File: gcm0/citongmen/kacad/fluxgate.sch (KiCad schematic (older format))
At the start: 81 parts, among them J1 +12, J11 SWD, J2 ji_li, Q1 BC547, Q10 KIA50N03, Q11 BC547, Q12 BC557, Q13 BC557, Q14 BC547, Q15 BC557, Q16 BC547, Q17 BC547, Q18 BC547, Q19 BC547, Q2 BC557, Q3 BC547, Q4 BC557, Q5 BC547, Q6 BC557, Q7 KIA50N03, Q8 KIA50N03, Q9 KIA50N03, U1 LM7809_TO220, U2 LM2596S-5, U3 LM7805_TO220, U5 STM32F030F4P6, U6 LM1117-3.3, U9 74HC595, Y1 8M

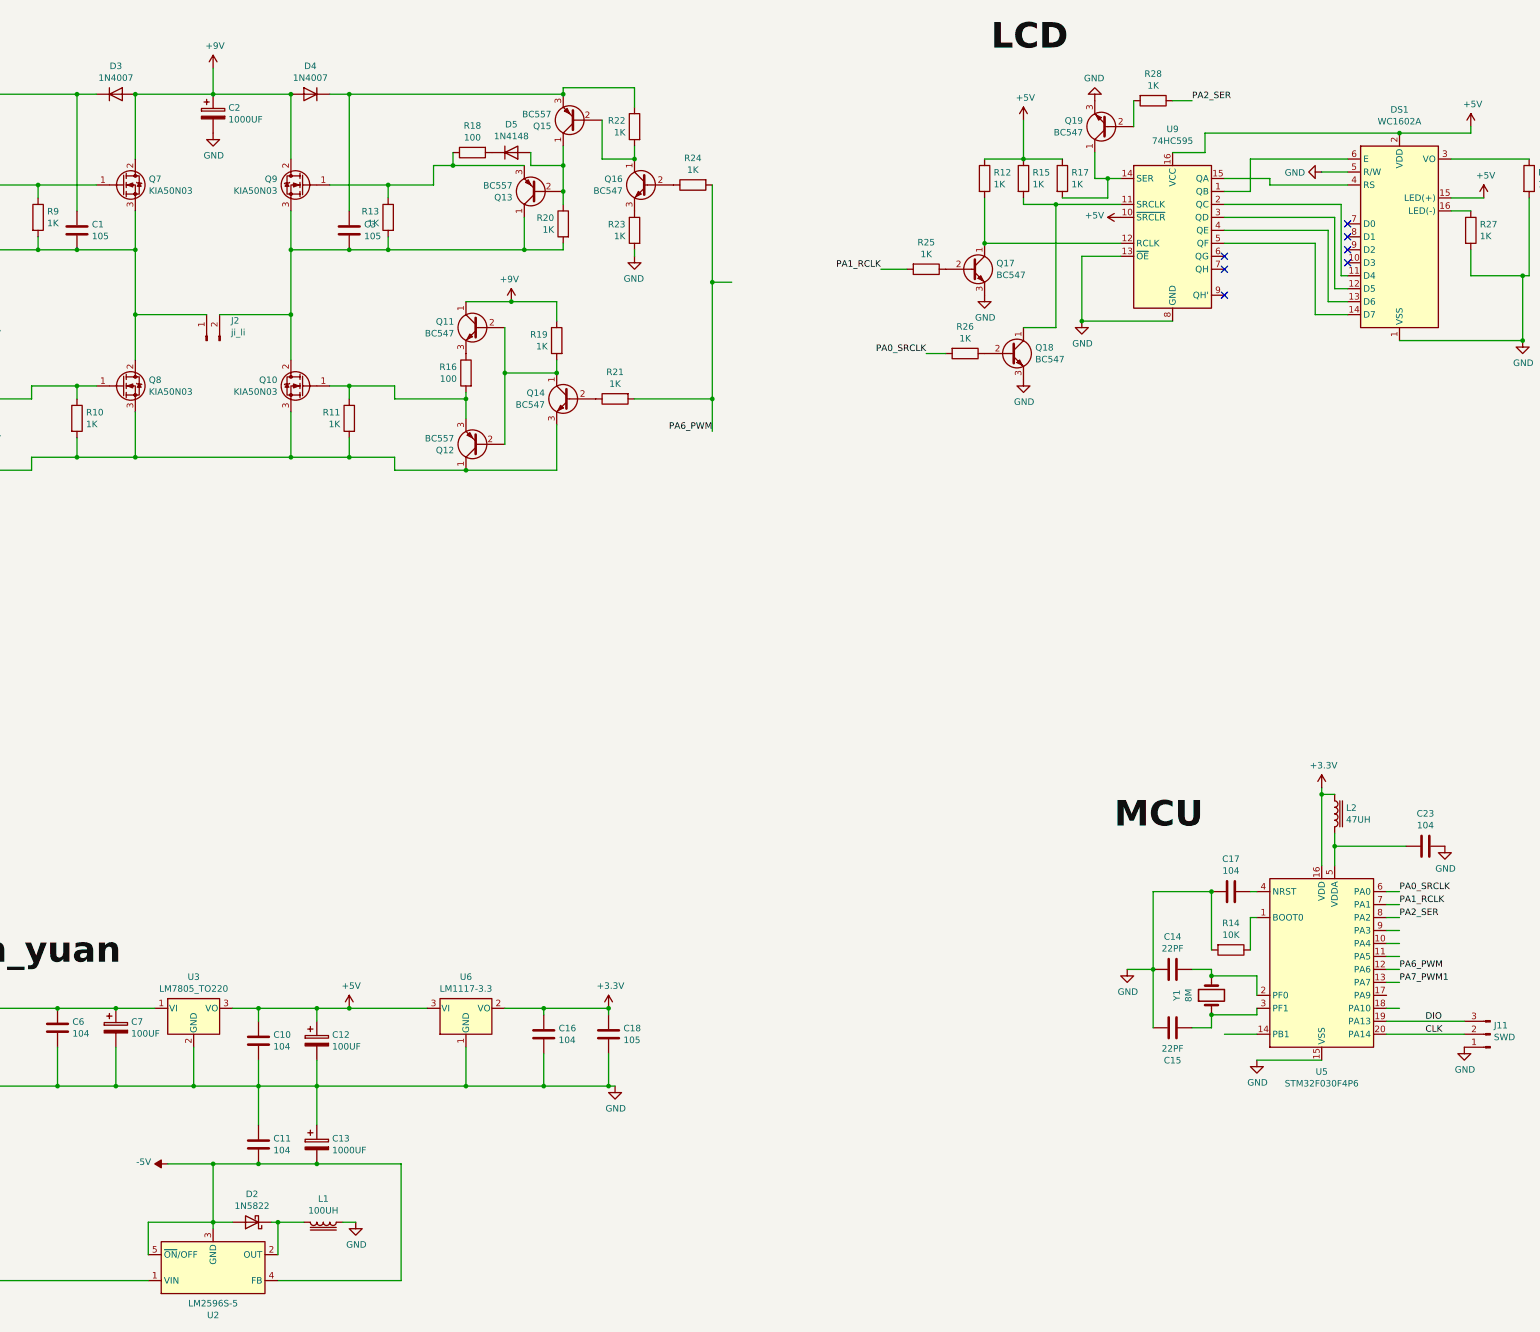
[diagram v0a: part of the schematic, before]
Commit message: 磁通门ADC采样
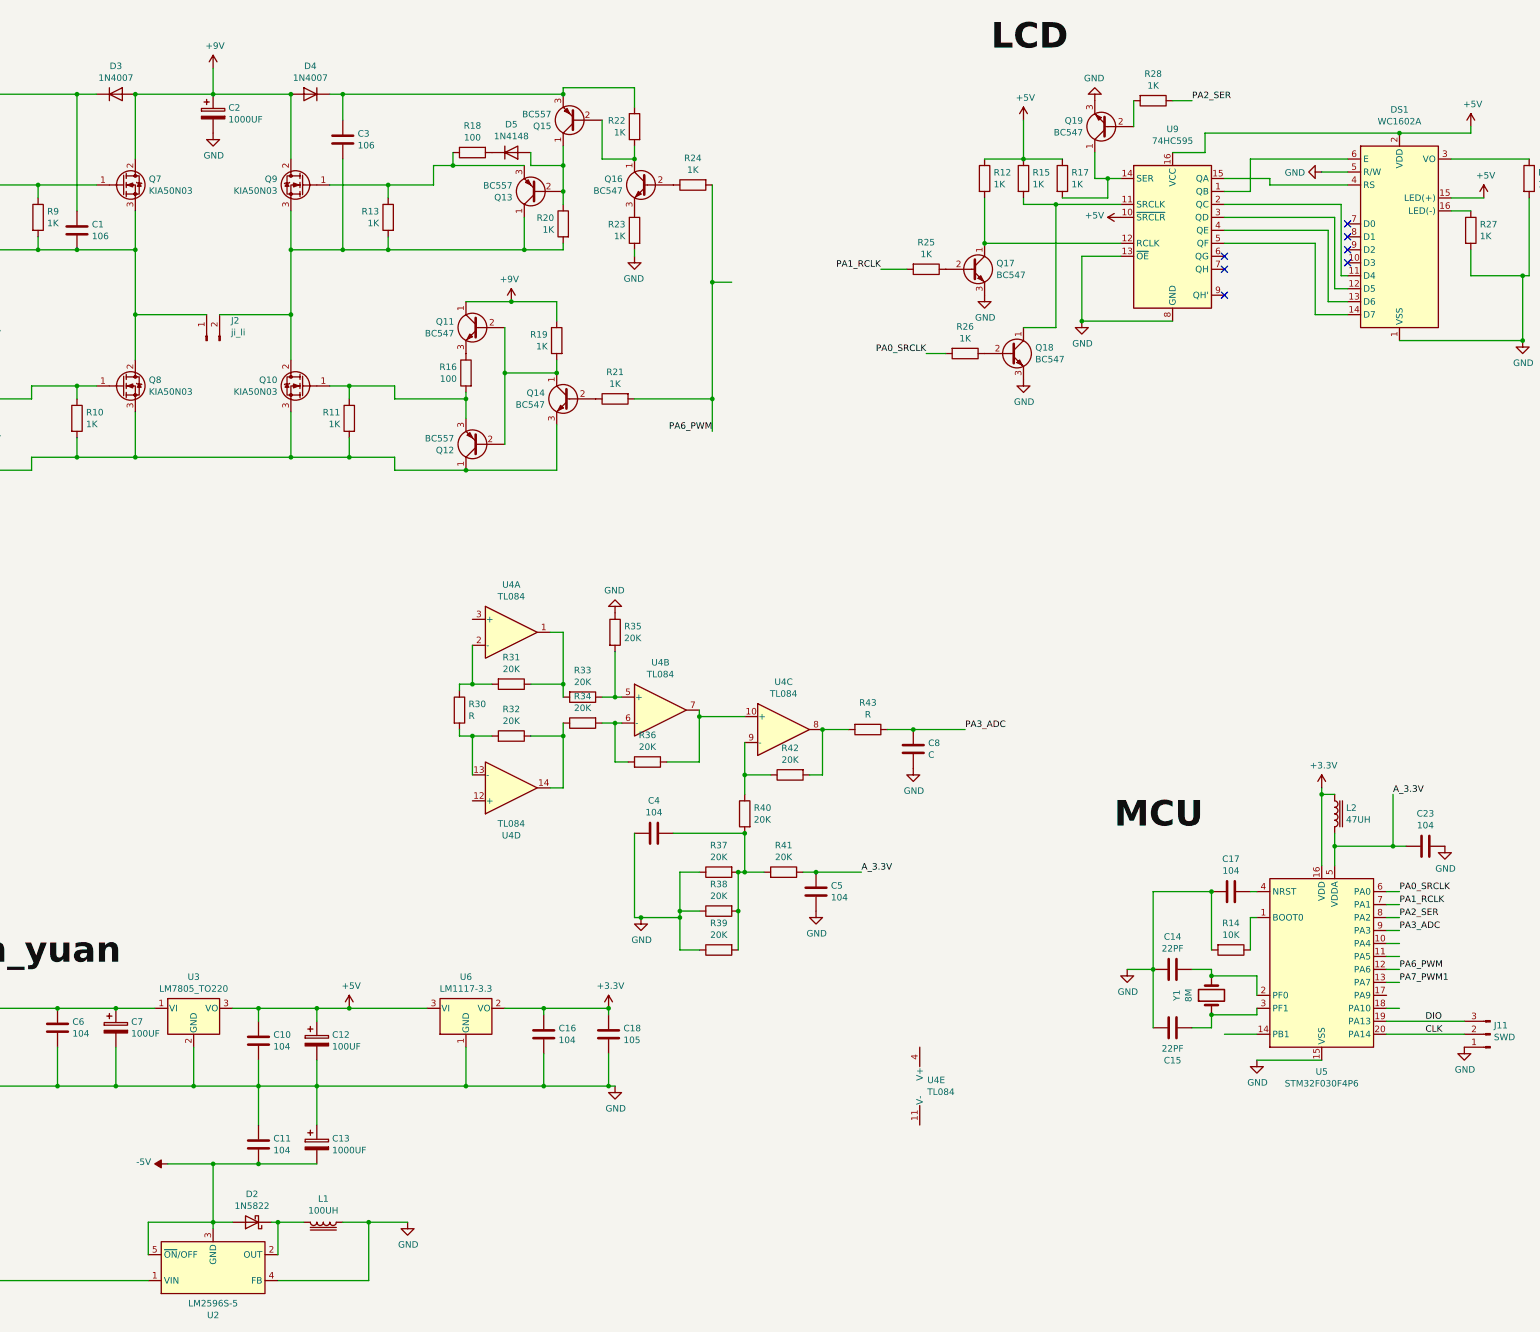
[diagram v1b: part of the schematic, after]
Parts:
- added C4, C5: 104, symbol Device:C
- added C8: C, symbol Device:C
- added R30, R43: R, symbol Device:R
- added R31, R32, R33, R34, R35, R36, R37, R38, R39, R40, R41, R42: 20K, symbol Device:R
- added U4: TL084, symbol Amplifier_Operational:TL084
- C1, C3: value 105 -> 106
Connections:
- net -5V: no longer U2.4 (FB)
- net GND: now also U2.4 (FB), C4.2, C5.1, C8.2, R35.1, R37.1, R38.1, R39.1
- net A_3.3V: now reaches C23.2, L2.2, U5.5 (VDDA)
- net A_3.3V: now also C5.2, R41.1
- net PA3_ADC: now reaches U5.9 (PA3)
- net PA3_ADC: now also C8.1, R43.1
- new net: R31.1, R33.2, U4.1
- new net: R30.1, R31.2, U4.2 (-)
- new net: R33.1, R35.2, U4.5 (+)
- new net: R34.2, R36.2, U4.6 (-)
- new net: R36.1, U4.10 (+), U4.7
- new net: R42.2, R43.2, U4.8
- new net: R40.1, R42.1, U4.9 (-)
- new net: R30.2, R32.2, U4.13 (-)
- new net: R32.1, R34.1, U4.14
- new net: C4.1, R37.2, R38.2, R39.2, R40.2, R41.2
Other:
- moved on the sheet: C3

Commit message: 删掉无用文件
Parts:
- added C?: 104, symbol Device:C
- added L?: 10, symbol Device:L_Core_Ferrite_Small
- added L? (x2): L, symbol Device:L
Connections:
- net GND: now also Q10.3 (S), Q12.1 (C), Q14.3 (E), Q3.3 (E), Q6.1 (C), Q8.3 (S), R10.2, R11.2, L?.1, L?.2
- net at C1.2, J2.1 (Pin_1), Q4.1 (C)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: now also L?.2
- net at U4.3 (+): now also C?.1, L?.2
- net at U4.12 (+): now also C?.2, L?.1
- net at C3.2, J2.2 (Pin_2), Q10.2 (D)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: now also L?.1
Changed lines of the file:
@@
 Connection ~ 8000 1300
 Wire Wire Line
-	4700 4100 5900 4100
+	4700 4100 4900 4100
 Connection ~ 4700 4100
 Connection ~ 5900 4100
@@
 	4700 2500 4700 3000
 Wire Wire Line
-	5250 3000 4700 3000
+	5250 3000 5000 3000
 Connection ~ 4700 3000
 Wire Wire Line
 	4700 3000 4700 3350
 Wire Wire Line
-	5350 3000 5900 3000
+	5350 3000 5650 3000
 Connection ~ 5900 3000
 Wire Wire Line
@@
 F 3 "~" H 8150 6150 50  0001 C CNN
 	1    8150 6150
-	0    -1   1    0
+	0    -1   -1   0
 $EndComp
 $Comp
@@
 F 3 "~" H 8650 6450 50  0001 C CNN
 	1    8650 6450
-	0    1    -1   0
+	0    1    1    0
 $EndComp
 Wire Wire Line
@@
 	9950 7300 10300 7300
 Connection ~ 9950 7300
+$Comp
+L Device:L_Core_Ferrite_Small L?
+U 1 1 60E8B5A8
+P 5350 4800
+F 0 "L?" V 5169 4800 50  0000 C CNN
+F 1 "10" V 5260 4800 50  0000 C CNN
+F 2 "" H 5350 4800 50  0001 C CNN
+F 3 "~" H 5350 4800 50  0001 C CNN
+	1    5350 4800
+	0    1    1    0
+$EndComp
+Wire Wire Line
+	5250 4800 5250 3300
+Wire Wire Line
+	5250 3300 5000 3300
+Wire Wire Line
+	5000 3300 5000 3000
+Connection ~ 5000 3000
+Wire Wire Line
+	5000 3000 4700 3000
+Wire Wire Line
+	5450 4800 5450 3700
+Wire Wire Line
+	5450 3700 5400 3700
+Wire Wire Line
+	5400 3700 5400 3350
+Wire Wire Line
+	5400 3350 5650 3350
+Wire Wire Line
+	5650 3350 5650 3000
+Connection ~ 5650 3000
+Wire Wire Line
+	5650 3000 5900 3000
+$Comp
+L Device:L L?
+U 1 1 60ECEB72
+P 5200 4900
+F 0 "L?" V 5390 4900 50  0000 C CNN
+F 1 "L" V 5299 4900 50  0000 C CNN
+F 2 "" H 5200 4900 50  0001 C CNN
+F 3 "~" H 5200 4900 50  0001 C CNN
+	1    5200 4900
+	0    -1   1    0
+$EndComp
+$Comp
+L Device:L L?
+U 1 1 60ED0F8B
+P 5500 4900
+F 0 "L?" V 5690 4900 50  0000 C CNN
+F 1 "L" V 5599 4900 50  0000 C CNN
+F 2 "" H 5500 4900 50  0001 C CNN
+F 3 "~" H 5500 4900 50  0001 C CNN
+	1    5500 4900
+	0    -1   1    0
+$EndComp
+Wire Wire Line
+	5350 4900 5350 5150
+Connection ~ 5350 4900
+$Comp
+L power:GND #PWR?
+U 1 1 60F5890A
+P 5350 5150
+F 0 "#PWR?" H 5350 4900 50  0001 C CNN
+F 1 "GND" H 5355 4977 50  0000 C CNN
+F 2 "" H 5350 5150 50  0001 C CNN
+F 3 "" H 5350 5150 50  0001 C CNN
+	1    5350 5150
+	1    0    0    -1
+$EndComp
+Wire Wire Line
+	5650 4900 5650 5350
+Wire Wire Line
+	5650 5350 7300 5350
+Wire Wire Line
+	5050 4900 5050 5800
+Wire Wire Line
+	5050 6750 7300 6750
+$Comp
+L Device:C C?
+U 1 1 60E8E98A
+P 5500 5800
+F 0 "C?" V 5248 5800 50  0000 C CNN
+F 1 "104" V 5339 5800 50  0000 C CNN
+F 2 "" H 5538 5650 50  0001 C CNN
+F 3 "~" H 5500 5800 50  0001 C CNN
+	1    5500 5800
+	0    1    1    0
+$EndComp
+Wire Wire Line
+	5650 5800 5650 5350
+Connection ~ 5650 5350
+Wire Wire Line
+	5350 5800 5050 5800
+Connection ~ 5050 5800
+Wire Wire Line
+	5050 5800 5050 6750
+$Comp
+L power:GND #PWR?
+U 1 1 60E90175
+P 4900 4100
+F 0 "#PWR?" H 4900 3850 50  0001 C CNN
+F 1 "GND" H 4905 3927 50  0000 C CNN
+F 2 "" H 4900 4100 50  0001 C CNN
+F 3 "" H 4900 4100 50  0001 C CNN
+	1    4900 4100
+	1    0    0    -1
+$EndComp
+Connection ~ 4900 4100
+Wire Wire Line
+	4900 4100 5900 4100
 $EndSCHEMATC

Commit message: 电路改错
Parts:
- removed C?: 104, symbol Device:C
- removed L?: 10, symbol Device:L_Core_Ferrite_Small
- removed L? (x2): L, symbol Device:L
- added C? (x3): C, symbol Device:C
- added U? (x3): NE5532, symbol Amplifier_Operational:NE5532
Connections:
- net +5V: now also U4.4 (V+), C?.2
- net -5V: now also U4.11 (V-), C?.2
- net GND: now also C?.1, C?.1
- net ji_li_0: now reaches C1.2, J2.1 (Pin_1), Q4.1 (C), Q7.3 (S), Q8.2 (D), R5.2, R9.2
- net at U4.3 (+): now also C?.1
- net at U4.12 (+): now also C?.2
- net ji_li_1: now reaches C3.2, J2.2 (Pin_2), Q10.2 (D), Q13.1 (C), Q9.3 (S), R13.2, R20.2
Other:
- moved on the sheet: C10, C11, C12, C13, C14, C15, C16, C17, C18, C23, C4, C5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

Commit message: PCB
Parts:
- removed C16, C23: 104, symbol Device:C
- removed C2: 1000UF, symbol Device:CP
- removed C? (x3): C, symbol Device:C
- removed J2: ji_li, symbol Connector:Conn_01x02_Male
- removed L2: 47UH, symbol Device:L_Core_Iron
- removed U1: LM7809_TO220, Package_TO_SOT_THT:TO-220-3_Vertical, symbol Regulator_Linear:LM7809_TO220
- added C19, C9: 105, Capacitor_SMD:C_0805_2012Metric_Pad1.18x1.45mm_HandSolder, symbol Device:C
- added C20, C21: 102, Capacitor_THT:C_Disc_D3.0mm_W2.0mm_P2.50mm, symbol Device:C
- added C26: 104, Capacitor_THT:C_Disc_D3.0mm_W2.0mm_P2.50mm, symbol Device:C
- added D6, D7, D8: 1N4007, Diode_THT:D_DO-41_SOD81_P10.16mm_Horizontal, symbol Diode:1N4007
- added J10, J12, J9: Conn_01x01_Male, Connector_Wire:SolderWirePad_1x01_SMD_1x2mm, symbol Connector:Conn_01x01_Male
- added J2, J3, J4, J5, J7, J8: Conn_01x01_Male, Connector_PinHeader_2.54mm:PinHeader_1x01_P2.54mm_Vertical, symbol Connector:Conn_01x01_Male
- added J6: GND, Connector_PinHeader_2.54mm:PinHeader_1x01_P2.54mm_Vertical, symbol Connector:Conn_01x01_Male
- added Q20, Q22: S8050, Package_TO_SOT_THT:TO-92_Inline_Wide, symbol Transistor_BJT:S8050
- added Q21, Q23: S8550, Package_TO_SOT_THT:TO-92_Inline_Wide, symbol Transistor_BJT:S8550
- added R44, R45: 100K, Resistor_THT:R_Axial_DIN0207_L6.3mm_D2.5mm_P5.08mm_Vertical, symbol Device:R
- added R46, R47, R48, R49: 1K, Resistor_THT:R_Axial_DIN0207_L6.3mm_D2.5mm_P5.08mm_Vertical, symbol Device:R
- C1, C14, C15, C18, C3: footprint (none) -> Capacitor_SMD:C_0805_2012Metric_Pad1.18x1.45mm_HandSolder
- C10, C11, C4, C5, C6: footprint (none) -> Capacitor_THT:C_Disc_D3.0mm_W2.0mm_P2.50mm
- C12, C13: footprint (none) -> Capacitor_THT:CP_Radial_D10.0mm_P3.50mm
- C17: footprint Capacitor_THT:C_Axial_L12.0mm_D6.5mm_P15.00mm_Horizontal -> Capacitor_THT:C_Disc_D3.0mm_W2.0mm_P2.50mm
- C7: value 100UF -> 1000UF; footprint (none) -> Capacitor_THT:CP_Radial_D10.0mm_P3.50mm
- C8: value C -> 104; footprint (none) -> Capacitor_THT:C_Disc_D3.0mm_W2.0mm_P2.50mm
- DS1: footprint Display:WC1602A -> Connector_PinHeader_2.54mm:PinHeader_1x16_P2.54mm_Vertical
- J1: footprint (none) -> Connector_PinHeader_2.54mm:PinHeader_1x01_P2.54mm_Vertical
- J11: footprint (none) -> Connector_PinHeader_2.54mm:PinHeader_1x03_P2.54mm_Vertical
- L1: footprint (none) -> Inductor_THT:L_Radial_D10.0mm_P5.00mm_Fastron_07P
- Q1, Q11, Q12, Q13, Q14, Q15, Q16, Q17, Q18, Q19, Q2, Q3, Q4, Q5, Q6: footprint Package_TO_SOT_THT:TO-92_Inline -> Package_TO_SOT_THT:TO-92_Inline_Wide
- Q10, Q7, Q8, Q9: footprint (none) -> Package_TO_SOT_SMD:TO-252-2
- R1, R10, R11, R13, R16, R18, R19, R2, R20, R21, R22, R23, R24, R25, R26, R28, R3, R31, R32, R33, R34, R35, R36, R37, R38, R39, R4, R40, R41, R42, R5, R6, R7, R8, R9: footprint (none) -> Resistor_THT:R_Axial_DIN0207_L6.3mm_D2.5mm_P5.08mm_Vertical
- R12, R14, R15, R17, R27, R29: footprint Resistor_THT:R_Axial_DIN0207_L6.3mm_D2.5mm_P10.16mm_Horizontal -> Resistor_THT:R_Axial_DIN0207_L6.3mm_D2.5mm_P5.08mm_Vertical
- R30: value R -> 5K; footprint (none) -> Resistor_THT:R_Axial_DIN0207_L6.3mm_D2.5mm_P5.08mm_Vertical
- R43: value R -> 100; footprint (none) -> Resistor_THT:R_Axial_DIN0207_L6.3mm_D2.5mm_P5.08mm_Vertical
- U4: footprint (none) -> Package_DIP:DIP-14_W7.62mm
- U6: footprint (none) -> Package_TO_SOT_SMD:SOT-223-3_TabPin2
- U7: renamed from U?; footprint (none) -> Package_DIP:DIP-8_W7.62mm
- Y1: footprint Crystal:Crystal_HC49-U_Vertical -> Crystal:Crystal_HC49-4H_Vertical
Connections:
- net +9V is gone; now on net +12V: D3.2 (A), D4.2 (A), Q11.1 (C), Q5.1 (C), Q7.2 (D), Q9.2 (D), R19.1, R6.1
- net +12V: now also D6.1 (K)
- net +3V3: now also U5.5 (VDDA)
- net +5V: now also U7.8 (V+), D8.1 (K), Q20.3 (C), Q22.3 (C); no longer DS1.15 (LED(+))
- net -5V: now also U7.4 (V-), D7.2 (A), Q21.3 (C), Q23.3 (C)
- net A_3.3V: no longer U5.5 (VDDA)
- net GND: now also C20.2, C21.1, C26.2, D6.2 (A), D7.1 (K), D8.2 (A), J6.1 (Pin_1), R44.2, R45.1; no longer C8.2
- net at U5.10 (PA4): now also J9.1 (Pin_1)
- net at U5.11 (PA5): now also J12.1 (Pin_1)
- net PB1_TIM1_CH3N: now reaches U5.14 (PB1)
- net PB1_TIM1_CH3N: now also C9.2
- net at U5.17 (PA9): now also J10.1 (Pin_1)
- net PA10_TIM1_CH3: now reaches U5.18 (PA10)
- net PA10_TIM1_CH3: now also C19.2
- net at U9.6 (QG): now also DS1.15 (LED(+))
- net chan_gan_qi_xin_hao-: now reaches U4.3 (+)
- net chan_gan_qi_xin_hao-: now also J4.1 (Pin_1)
- net chuan_gan_qi_xin_hao+: now reaches U4.12 (+)
- net chuan_gan_qi_xin_hao+: now also J8.1 (Pin_1)
- net at U7.1: now also R49.2
- net dian_ci_bu_chang+: now reaches U7.2 (-)
- net dian_ci_bu_chang+: now also J7.1 (Pin_1), Q22.1 (E), Q23.1 (E)
- net at U7.3 (+): now also C21.2, R47.1
- net at U7.5 (+): now also C20.1, R46.1
- net dian_ci_bu_chang-: now reaches U7.6 (-)
- net dian_ci_bu_chang-: now also J3.1 (Pin_1), Q20.1 (E), Q21.1 (E)
- net at U7.7: now also R48.2
- net ji_li_0 renamed A
- net A: now also J2.1 (Pin_1)
- net ji_li_1 renamed B
- net B: now also J5.1 (Pin_1)
- new net: C26.1, C8.2
- new net: Q22.2 (B), Q23.2 (B), R49.1
- new net: Q20.2 (B), Q21.2 (B), R48.1
- new net: C9.1, R44.1, R46.2
- new net: C19.1, R45.2, R47.2
- no-connect marks 7 -> 6
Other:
- moved on the sheet: C6, C7, U7A, U7B, U7C
